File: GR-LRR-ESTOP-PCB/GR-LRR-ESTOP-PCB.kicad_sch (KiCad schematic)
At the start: 2 parts

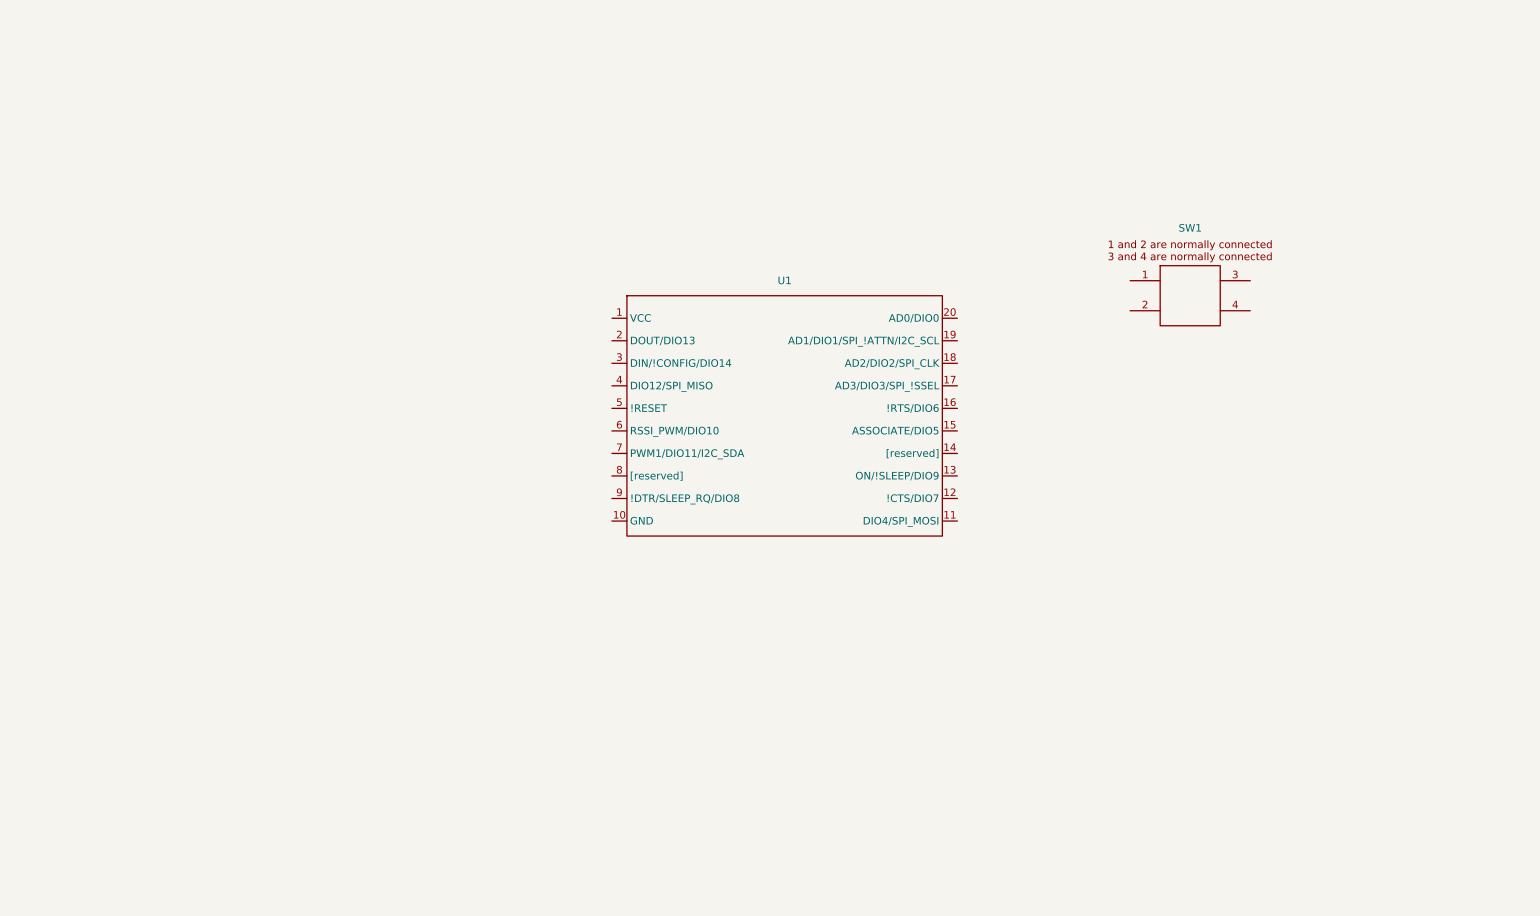
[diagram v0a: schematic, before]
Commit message: moving to two enclosures
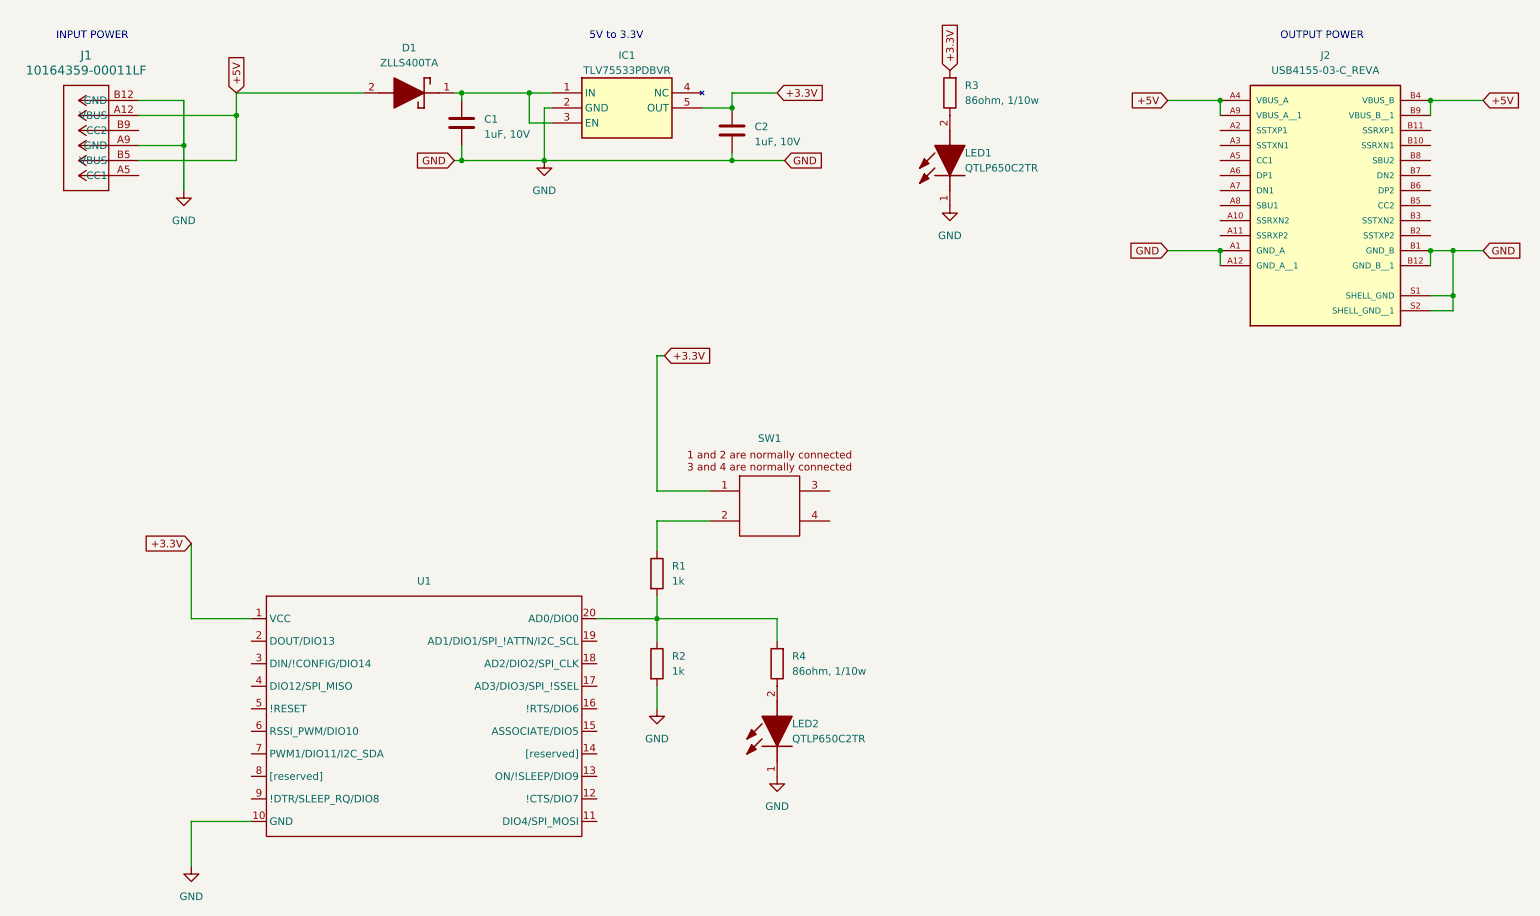
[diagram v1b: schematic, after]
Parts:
- added C1, C2: 1uF, 10V, Capacitor_SMD:C_0805_2012Metric_Pad1.18x1.45mm_HandSolder, symbol Device:C
- added D1: ZLLS400TA, SOD2513X120N, symbol ZLLS400TA:ZLLS400TA
- added IC1: TLV75533PDBVR, SOT95P280X145-5N, symbol TLV75533PDBVR:TLV75533PDBVR
- added J1: 10164359-00011LF, 10164359_00011LF:CONN_10164359-00011LF_AMP, symbol 10164359_00011LF:10164359-00011LF
- added J2: USB4155-03-C_REVA, USB4155_03_C:GCT_USB4155-03-C_REVA, symbol USB4155-03-C_REVA:USB4155-03-C_REVA
- added LED1, LED2: QTLP650C2TR, QTLP650C2TR:LEDC3216X130N, symbol QTLP650C2TR:QTLP650C2TR
- added R1, R2: 1k, Resistor_SMD:R_1206_3216Metric_Pad1.30x1.75mm_HandSolder, symbol Device:R
- added R3, R4: 86ohm, 1/10w, Resistor_SMD:R_1206_3216Metric_Pad1.30x1.75mm_HandSolder, symbol Device:R
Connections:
- net +3.3V: now reaches SW1.1
- net +3.3V: now also U1.1 (VCC), C2.1, IC1.5 (OUT), R3.2
- net at SW1.2: now also R1.1
- net GND: now reaches U1.10 (GND)
- net GND: now also C1.2, C2.2, IC1.2 (GND), J1.A9 (GND), J1.B12 (GND), J2.A1 (GND_A), J2.A12 (GND_A__1), J2.B1 (GND_B), J2.B12 (GND_B__1), J2.S1 (SHELL_GND), J2.S2 (SHELL_GND__1), LED1.1 (K), LED2.1 (K), R2.2
- net at U1.20 (AD0/DIO0): now also R1.2, R2.1, R4.2
- new net: LED2.2 (A), R4.1
- new net: C1.1, D1.1 (K), IC1.1 (IN), IC1.3 (EN)
- new net: LED1.2 (A), R3.1
- new net +5V: D1.2 (A), J1.A12 (VBUS), J1.B5 (VBUS), J2.A4 (VBUS_A), J2.A9 (VBUS_A__1), J2.B4 (VBUS_B), J2.B9 (VBUS_B__1)
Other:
- note added: "5V to 3.3V"
- note added: "INPUT POWER"
- note added: "OUTPUT POWER"
- moved on the sheet: SW1, U1
